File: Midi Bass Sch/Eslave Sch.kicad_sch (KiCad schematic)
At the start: 5 parts

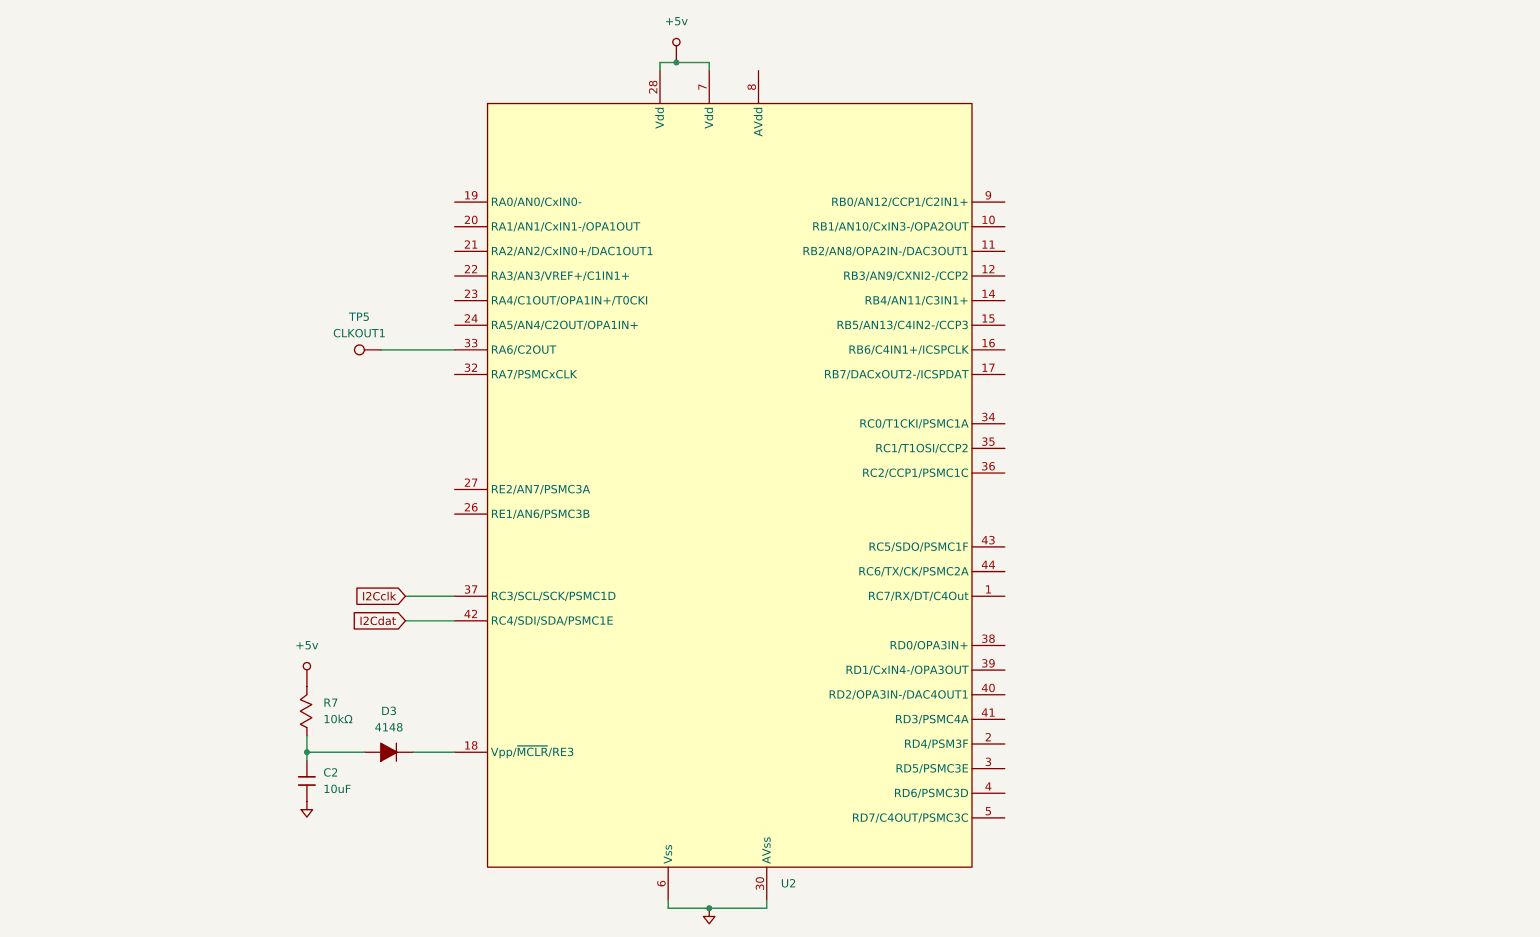
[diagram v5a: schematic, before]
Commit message: changed schematic for e slave to be a 1788 and now has status leds
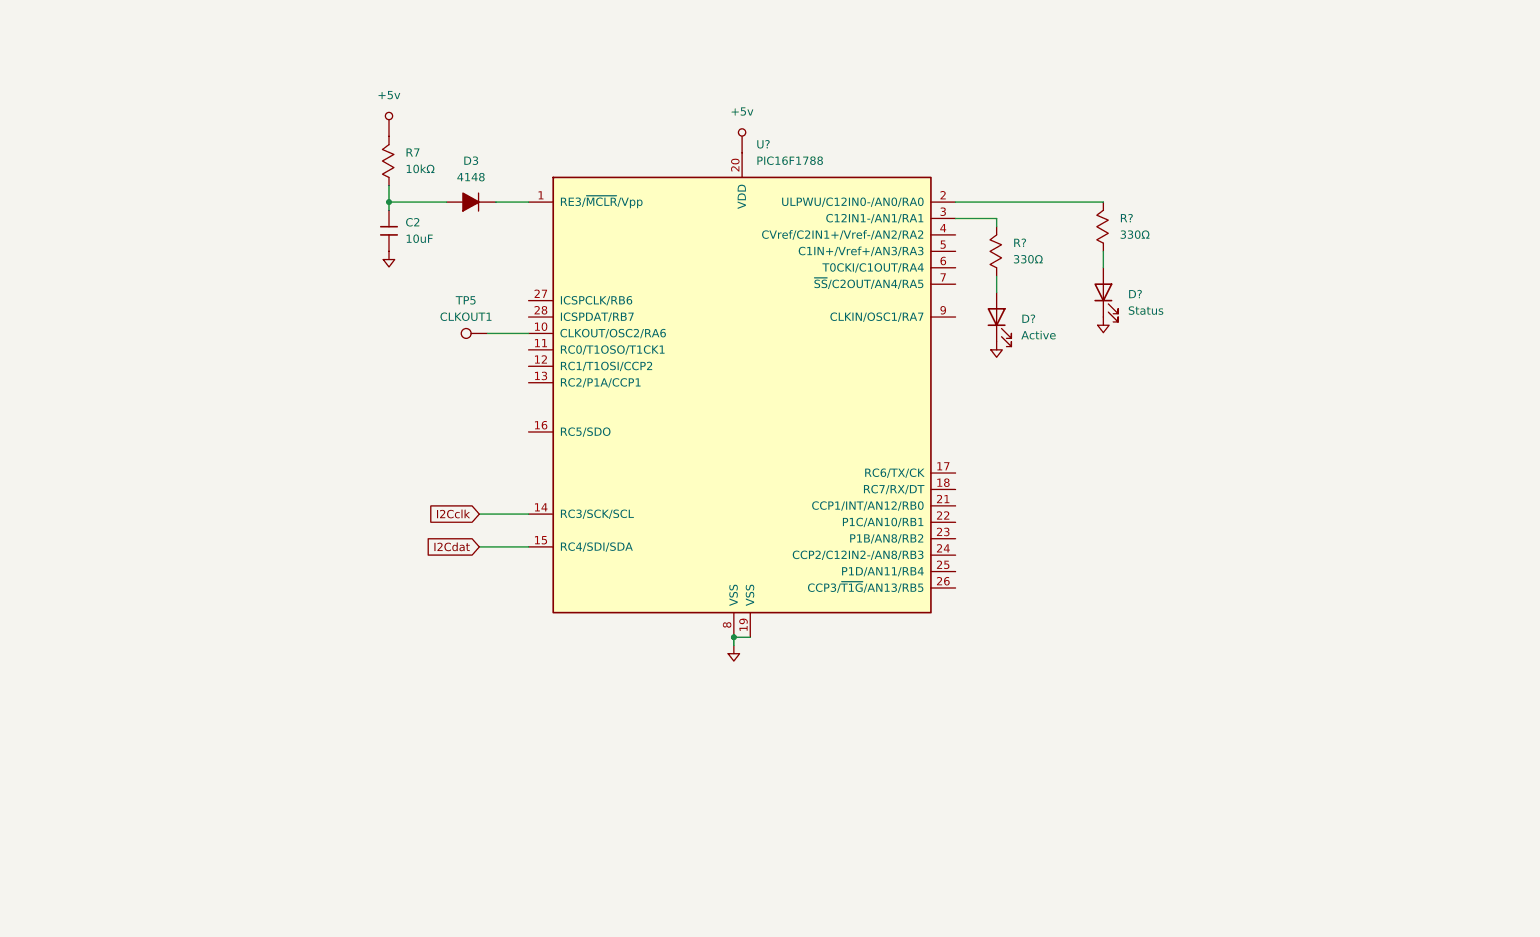
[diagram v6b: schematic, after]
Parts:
- removed U2: ~, symbol Owen's Symbols:PIC16F1789_44
- added D?: Active, symbol Device:LED
- added D?: Status, symbol Device:LED
- added R? (x2): 330Ω, symbol Owen's Symbols:Resistor_Mod
- added U?: PIC16F1788, symbol Owen's Symbols:PIC16F1788_2
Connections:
- net +5v: now also U?.20 (VDD)
- net GND: now also D?.1 (K), D?.1 (K), U?.19 (VSS), U?.8 (VSS)
- net I2Cclk: now also U?.14 (RC3/SCK/SCL)
- net I2Cdat: now also U?.15 (RC4/SDI/SDA)
- net at TP5.1: now also U?.10 (CLKOUT/OSC2/RA6)
- net at D3.2: now also U?.1 (RE3/~{MCLR}/Vpp)
- new net: D?.2 (A), R?.1 (x2)
- new net: R?.2, U?.2 (ULPWU/C12IN0-/AN0/RA0)
- new net: R?.2, U?.3 (C12IN1-/AN1/RA1)
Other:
- moved on the sheet: C2, D3, R7, TP5

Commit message: Added stepper controller to E slave
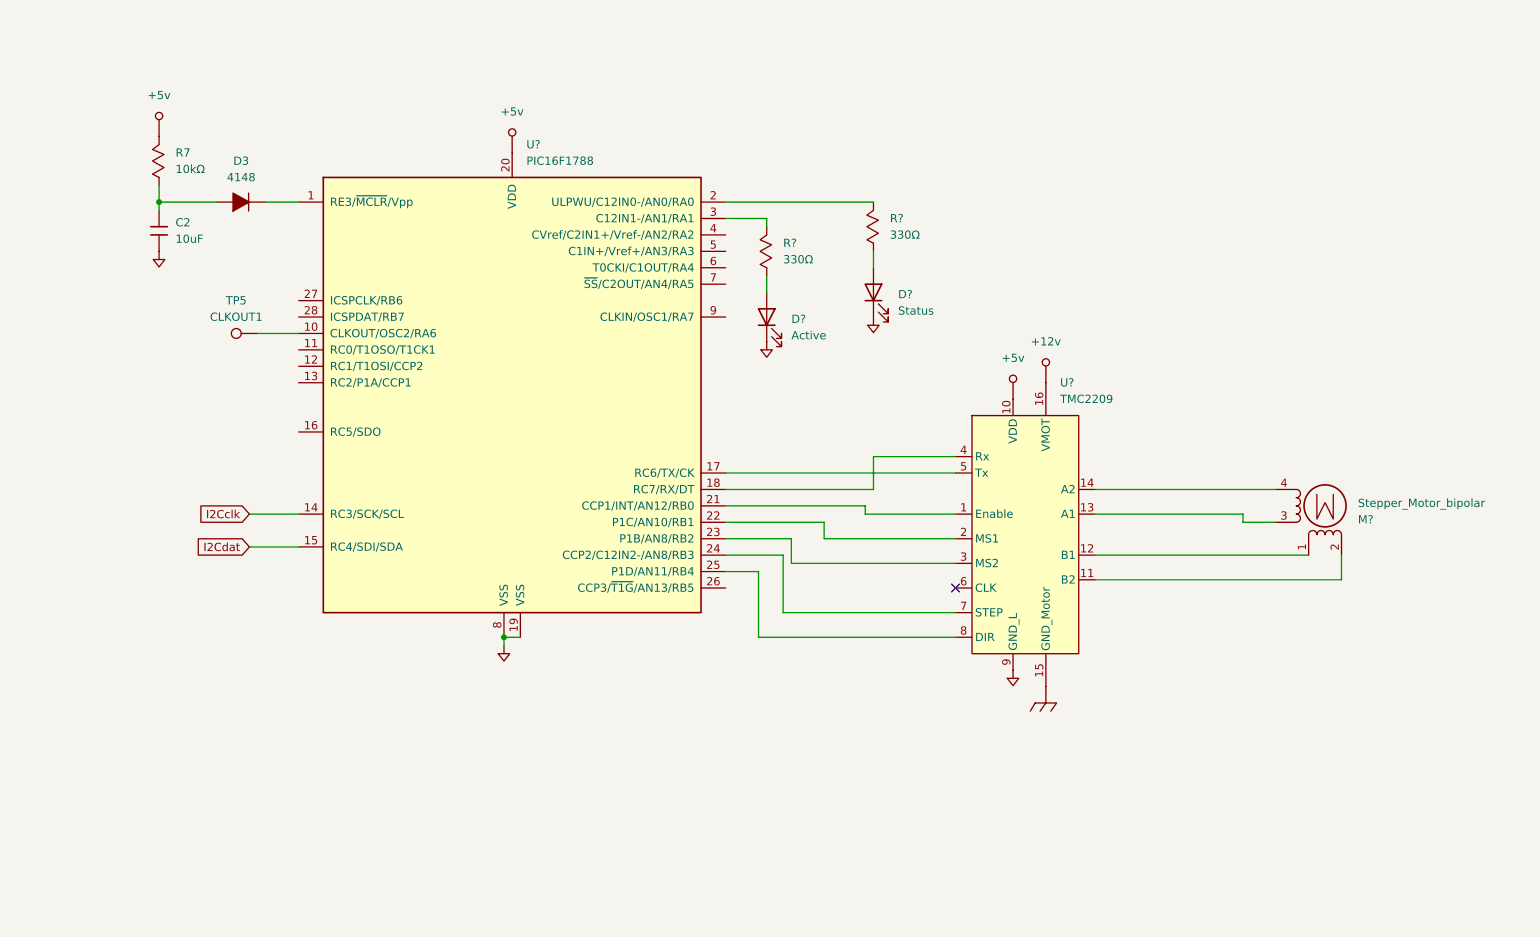
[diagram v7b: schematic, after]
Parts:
- added M?: Stepper_Motor_bipolar, symbol Motor:Stepper_Motor_bipolar
- added U?: TMC2209, symbol Digital ICS:TMC2209
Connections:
- net +5v: now also U?.10 (VDD)
- net GND: now also U?.9 (GND_L)
- net at U?.17 (RC6/TX/CK): now also U?.5 (Tx)
- net at U?.18 (RC7/RX/DT): now also U?.4 (Rx)
- net at U?.21 (CCP1/INT/AN12/RB0): now also U?.1 (Enable)
- net at U?.22 (P1C/AN10/RB1): now also U?.2 (MS1)
- net at U?.23 (P1B/AN8/RB2): now also U?.3 (MS2)
- net at U?.24 (CCP2/C12IN2-/AN8/RB3): now also U?.7 (STEP)
- net at U?.25 (P1D/AN11/RB4): now also U?.8 (DIR)
- new net: M?.2 (-), U?.11 (B2)
- new net: M?.1, U?.12 (B1)
- new net: M?.3, U?.13 (A1)
- new net: M?.4, U?.14 (A2)
- new net +12v: U?.16 (VMOT)
- new net Chassis_GND: U?.15 (GND_Motor)
- no-connect marks 0 -> 1
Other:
- moved on the sheet: C2, D3, D?, R7, R?, TP5, U?

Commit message: updated e slave added solenoid for slave added reset button
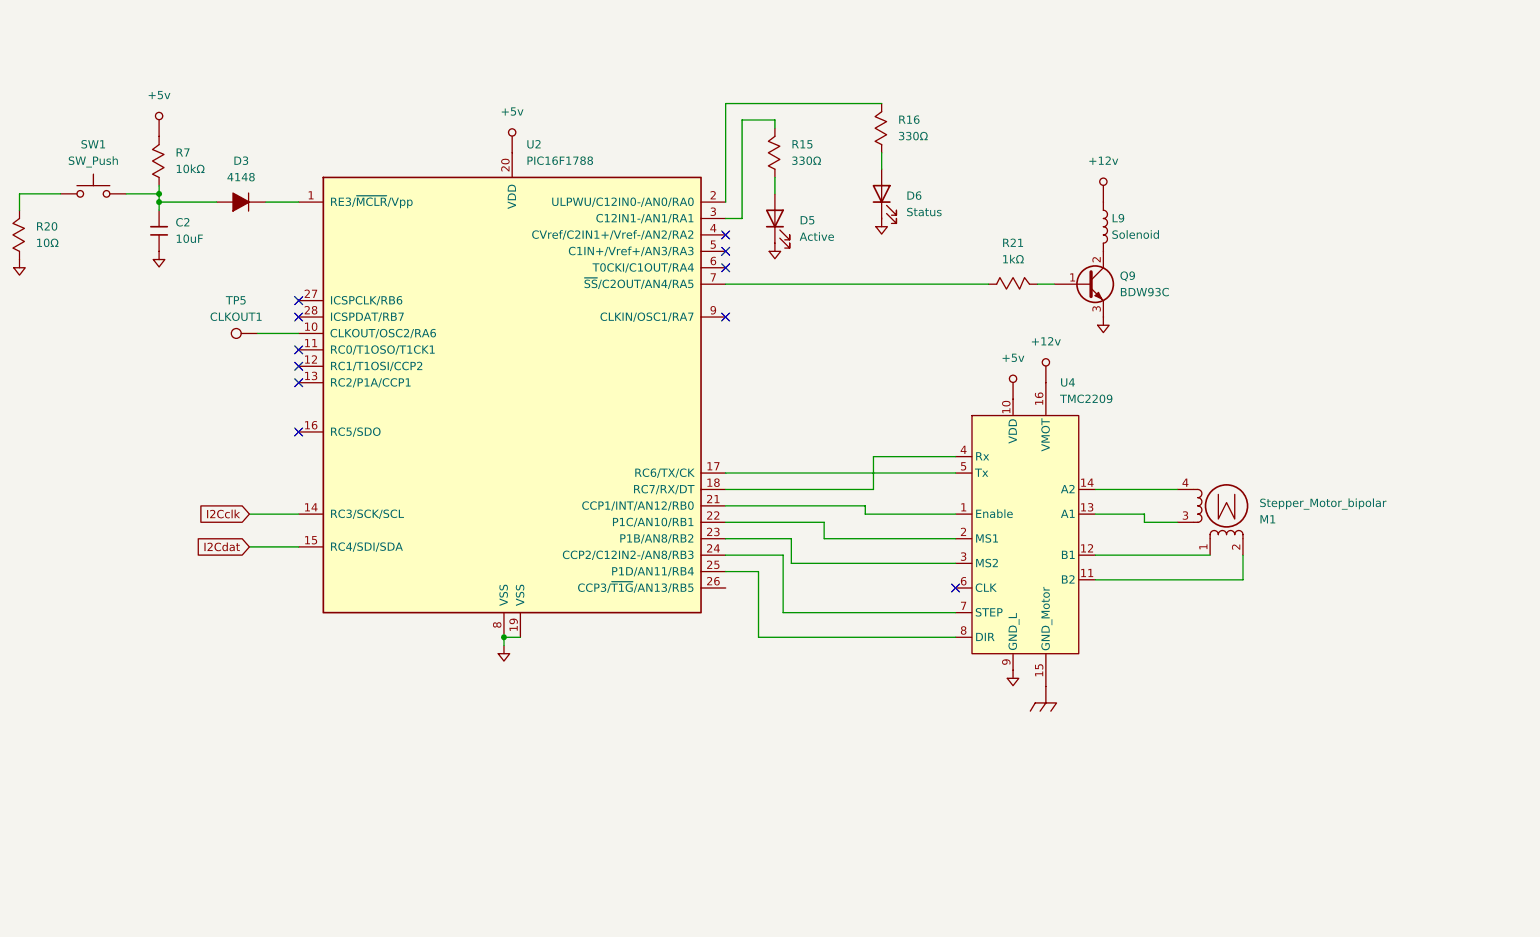
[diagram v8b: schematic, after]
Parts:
- added L9: Solenoid, symbol Device:L
- added Q9: BDW93C, symbol Device:Q_NPN_BCE
- added R20: 10Ω, symbol Owen's Symbols:Resistor_Mod
- added R21: 1kΩ, symbol Custom Symbols:Resistor_Mod
- added SW1: SW_Push, symbol Switch:SW_Push
- gave numbers to parts that had none: 7
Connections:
- net +12v: now also L9.1
- net GND: now also Q9.3 (E), R20.1
- net at C2.1, D3.1, R7.1: now also SW1.2
- net at U2.7 (~{SS}/C2OUT/AN4/RA5): now also R21.1
- new net: L9.2, Q9.2 (C)
- new net: R20.2, SW1.1
- new net: Q9.1 (B), R21.2
- no-connect marks 1 -> 11
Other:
- moved on the sheet: D5, D6, M1, R15, R16
